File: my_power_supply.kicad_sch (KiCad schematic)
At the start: 61 parts, among them J1 USB_C_Receptacle_USB2.0_16P, J2 USB_C_Receptacle_PowerOnly_6P, J3 USB_C_Receptacle_PowerOnly_6P, Q1 DMP3013SFV, Q2 DMP3013SFV, SW1 SW_SPST, SW2 SW_SPST, U1 CYPD3177-24LQ, U2 TPS54560BDDA, U3 TPS54560BDDA

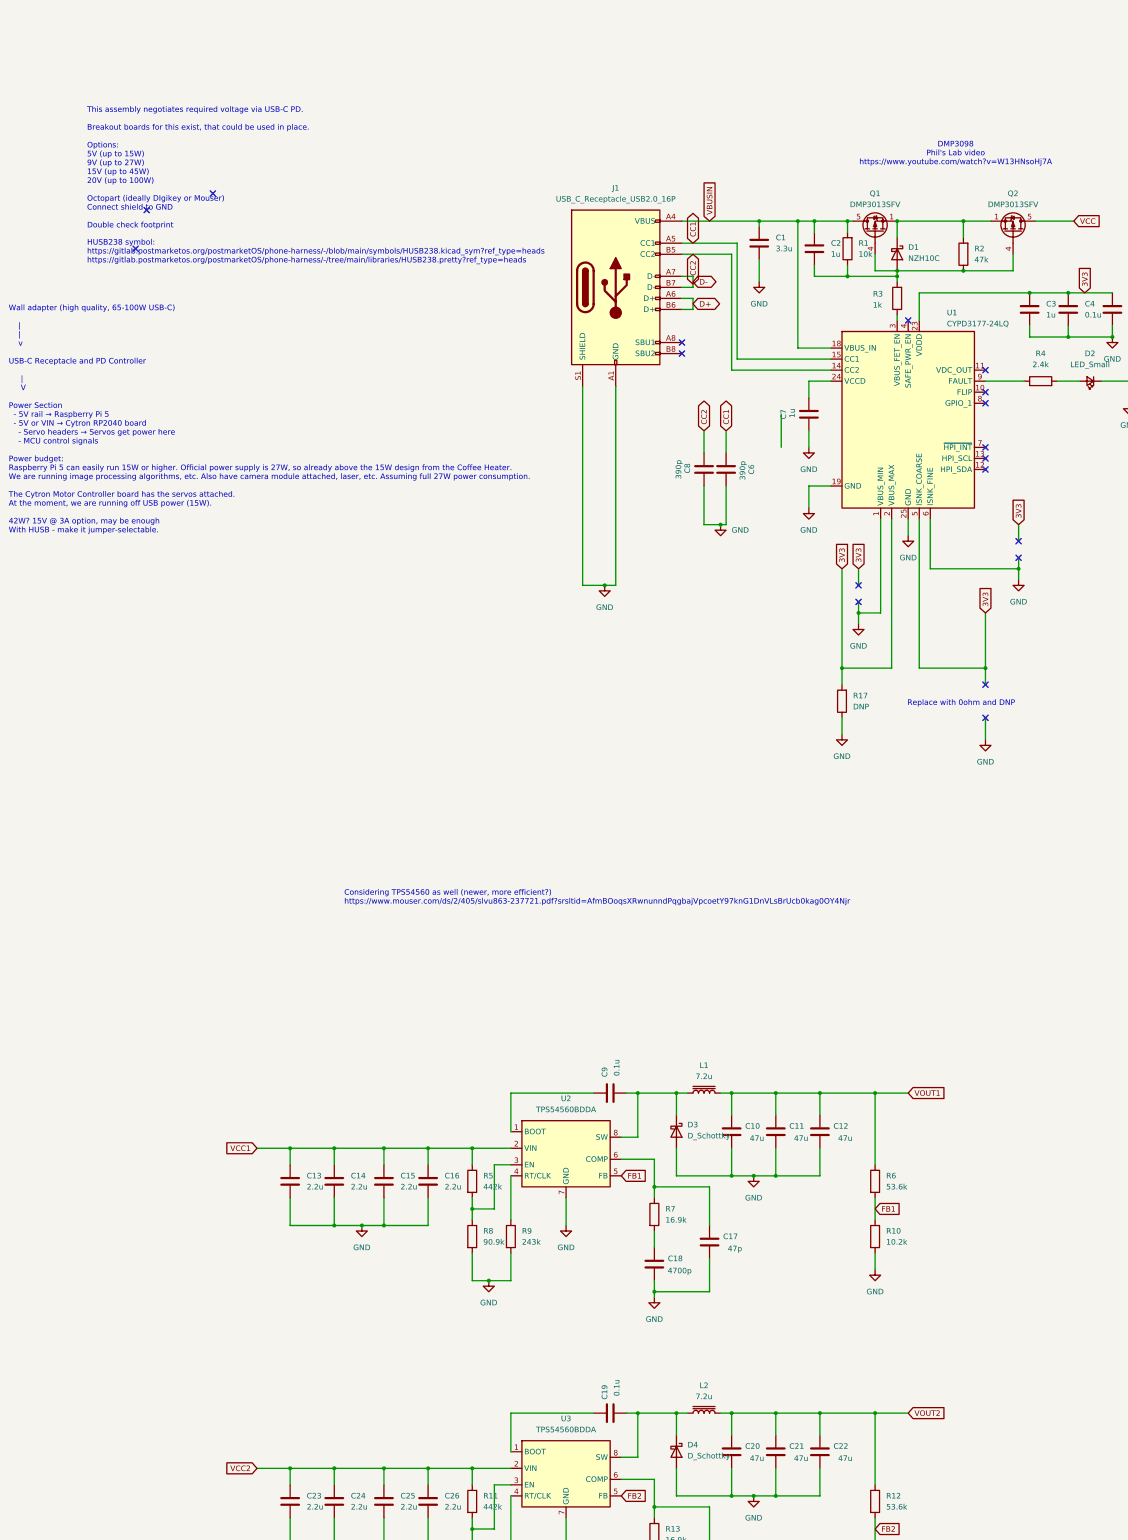
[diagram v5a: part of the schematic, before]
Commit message: Voltage/Current setting resistors use DNF and 0
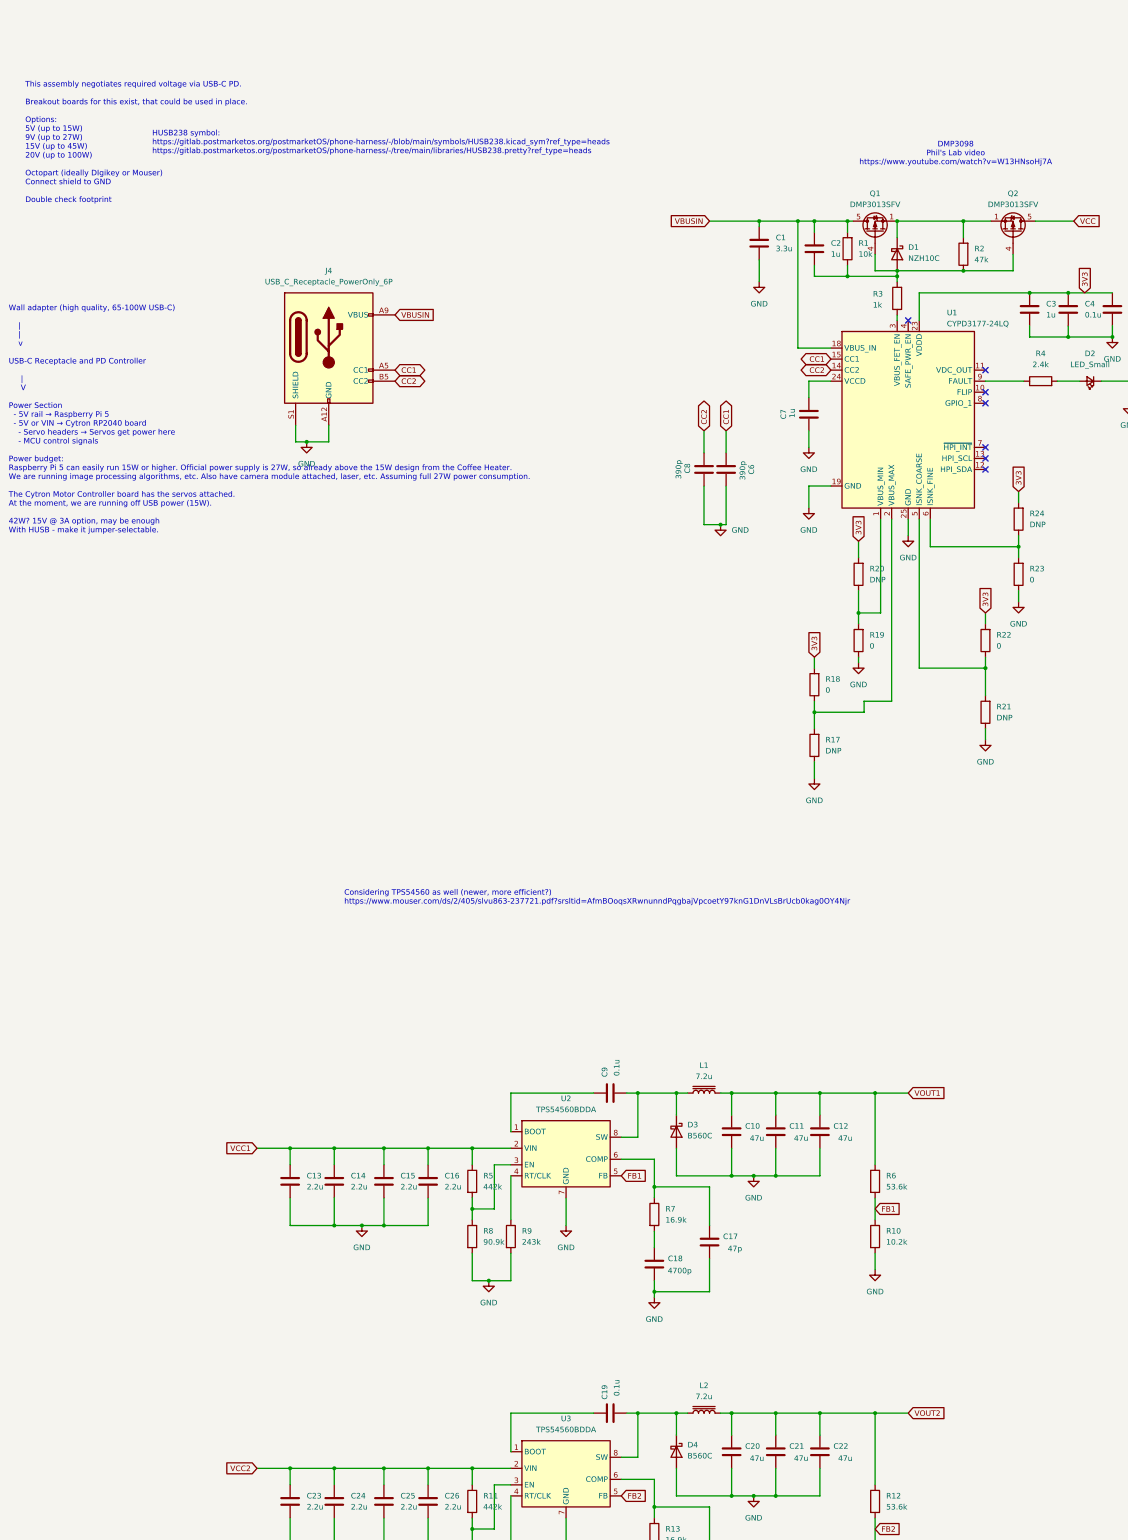
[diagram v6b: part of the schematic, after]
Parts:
- removed J1: USB_C_Receptacle_USB2.0_16P, Connector_USB:USB_C_Plug_JAE_DX07P024AJ1, symbol Connector:USB_C_Receptacle_USB2.0_16P
- added J4: USB_C_Receptacle_PowerOnly_6P, Connector_USB:USB_C_Plug_Molex_105444, symbol Connector:USB_C_Receptacle_PowerOnly_6P
- added R18, R19, R22, R23: 0, Resistor_SMD:R_0805_2012Metric, symbol Device:R
- added R20, R21, R24: DNP, Resistor_SMD:R_0805_2012Metric, symbol Device:R
- D3, D4: value D_Schottky -> B560C
- R17: footprint Resistor_SMD:R_1206_3216Metric -> Resistor_SMD:R_0805_2012Metric
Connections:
- net 3V3: now also R18.2, R20.2, R22.2, R24.2; no longer R17.2, U1.2 (VBUS_MAX), U1.5 (ISNK_COARSE)
- net CC1: now also J4.A5 (CC1)
- net CC2: now also J4.B5 (CC2)
- net GND: now also J4.A12 (GND), J4.B12 (GND), J4.S1 (SHIELD), R19.1, R21.1, R23.1; no longer U1.1 (VBUS_MIN), U1.6 (ISNK_FINE)
- net VBUSIN: now also J4.A9 (VBUS), J4.B9 (VBUS)
- new net: R19.2, R20.1, U1.1 (VBUS_MIN)
- new net: R17.2, R18.1, U1.2 (VBUS_MAX)
- new net: R21.2, R22.1, U1.5 (ISNK_COARSE)
- new net: R23.2, R24.1, U1.6 (ISNK_FINE)
- no-connect marks 22 -> 11
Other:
- note removed: "Replace with 0ohm and DNP"
- moved on the sheet: R17
